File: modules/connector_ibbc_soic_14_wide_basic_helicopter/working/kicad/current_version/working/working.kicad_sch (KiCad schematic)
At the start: 1 part, among them U1 insoic14wi2cheli

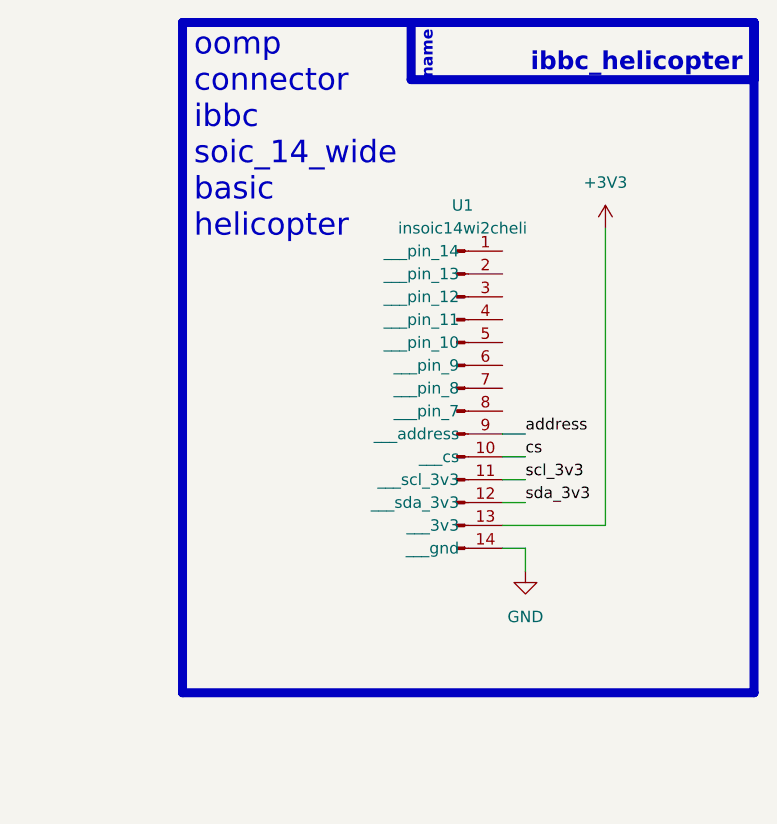
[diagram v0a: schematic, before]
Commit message: fixed formatting to be more consistent
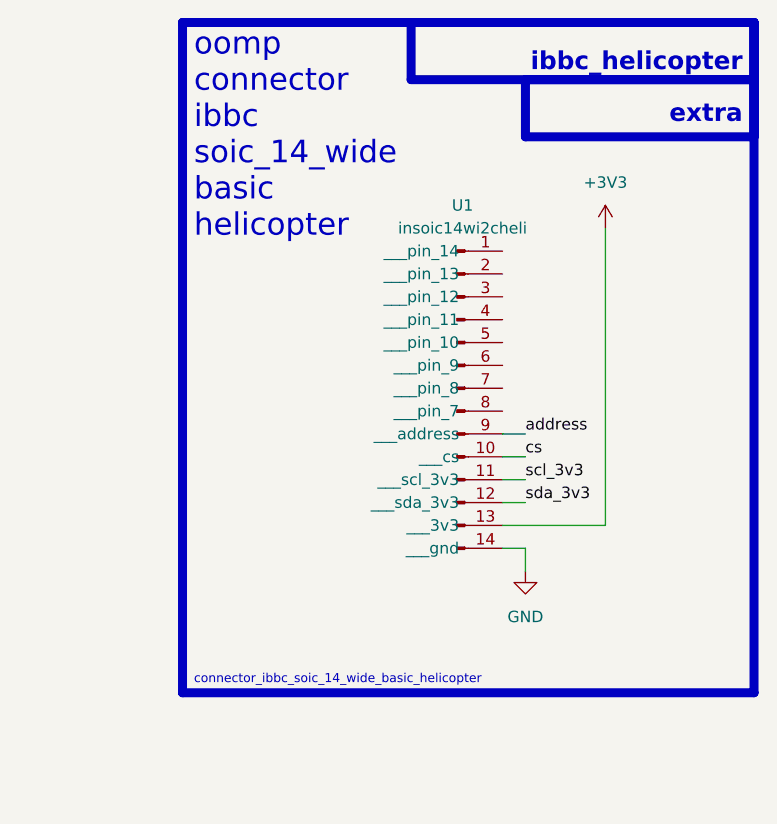
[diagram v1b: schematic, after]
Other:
- note added: "connector_ibbc_soic_14_wide_basic_helicopter"
- note added: "extra"
- note removed: "name"
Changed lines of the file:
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@@
     (stroke (width 0) (type default))
+  )
+  (rectangle (start 132.08 24.13) (end 157.48 30.48)
+    (stroke (width 1) (type default))
+    (fill (type none))
   )
   (rectangle (start 93.98 17.78) (end 157.48 92.2532)
@@
   (rectangle (start 119.38 17.78) (end 157.48 24.13)
     (stroke (width 1) (type default))
-    (fill (type color) (color 0 0 0 0))
+    (fill (type none))
   )
   (text "ibbc_helicopter\n\n" (at 156.21 26.67 0)
-    (effects (font (size 2 2) (thickness 0.8) bold (color 255 255 255 1)) (justify right bottom))
-  )
-  (text "name" (at 121.92 24.13 90)
-    (effects (font (size 1.27 1.27) (thickness 0.254) bold (color 255 255 255 1)) (justify left bottom))
+    (effects (font (size 2 2) (thickness 0.8) bold) (justify right bottom))
   )
   (text "oomp\nconnector\nibbc\nsoic_14_wide\nbasic\nhelicopter\n"
@@
     (effects (font (size 2.5 2.5)) (justify left bottom))
   )
+  (text "extra" (at 156.21 29.21 0)
+    (effects (font (size 2 2) (thickness 0.8) bold) (justify right bottom))
+  )
+  (text "connector_ibbc_soic_14_wide_basic_helicopter" (at 95.25 91.44 0)
+    (effects (font (size 1 1)) (justify left bottom))
+  )
   (label "cs" (at 132.08 66.04 0) (fields_autoplaced)

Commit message: schematic formatting
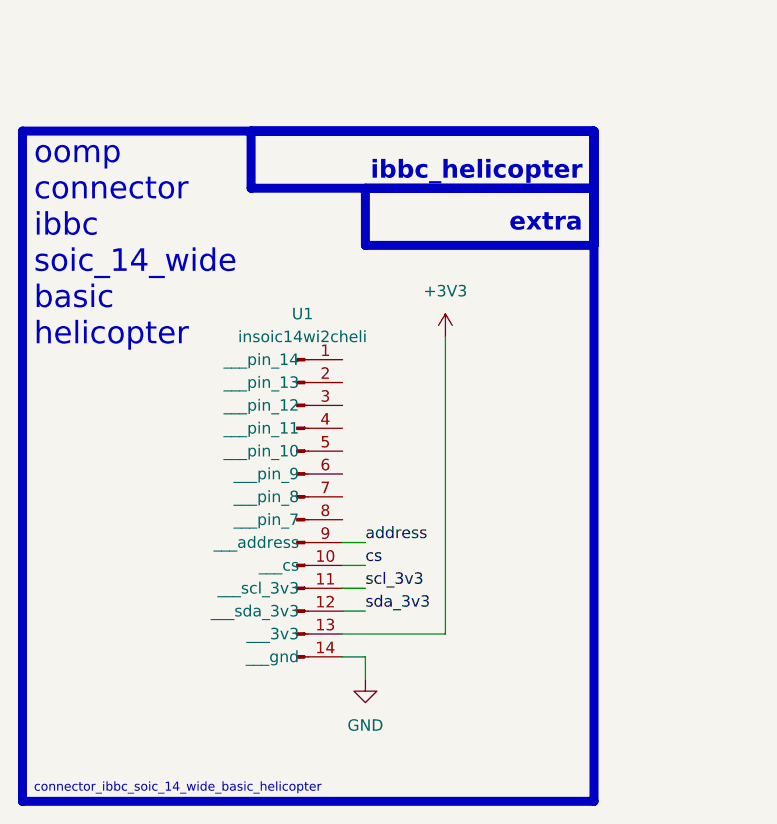
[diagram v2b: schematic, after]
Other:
- moved on the sheet: U1
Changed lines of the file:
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@@
 (kicad_sch (version 20230121) (generator eeschema)
-  (paper "A4")
-  (wire (pts (xy 140.97 73.66) (xy 129.54 73.66))
+  (paper "A5")
+  (wire (pts (xy 123.19 85.725) (xy 111.76 85.725))
     (stroke (width 0) (type default))
   )
-  (wire (pts (xy 129.54 66.04) (xy 132.08 66.04))
+  (wire (pts (xy 111.76 78.105) (xy 114.3 78.105))
     (stroke (width 0) (type default))
   )
-  (wire (pts (xy 129.54 63.5) (xy 132.08 63.5))
+  (wire (pts (xy 111.76 75.565) (xy 114.3 75.565))
     (stroke (width 0) (type default))
   )
-  (wire (pts (xy 140.97 40.64) (xy 140.97 73.66))
+  (wire (pts (xy 123.19 52.705) (xy 123.19 85.725))
     (stroke (width 0) (type default))
   )
-  (wire (pts (xy 129.54 71.12) (xy 132.08 71.12))
+  (wire (pts (xy 111.76 83.185) (xy 114.3 83.185))
     (stroke (width 0) (type default))
   )
-  (wire (pts (xy 132.08 76.2) (xy 129.54 76.2))
+  (wire (pts (xy 114.3 88.265) (xy 111.76 88.265))
     (stroke (width 0) (type default))
   )
-  (wire (pts (xy 132.08 78.74) (xy 132.08 76.2))
+  (wire (pts (xy 114.3 90.805) (xy 114.3 88.265))
     (stroke (width 0) (type default))
   )
-  (wire (pts (xy 129.54 68.58) (xy 132.08 68.58))
+  (wire (pts (xy 111.76 80.645) (xy 114.3 80.645))
     (stroke (width 0) (type default))
   )
-  (rectangle (start 132.08 24.13) (end 157.48 30.48)
+  (rectangle (start 114.3 36.195) (end 139.7 42.545)
     (stroke (width 1) (type default))
     (fill (type none))
   )
-  (rectangle (start 93.98 17.78) (end 157.48 92.2532)
+  (rectangle (start 76.2 29.845) (end 139.7 104.3182)
     (stroke (width 1) (type default))
     (fill (type none))
   )
-  (rectangle (start 119.38 17.78) (end 157.48 24.13)
+  (rectangle (start 101.6 29.845) (end 139.7 36.195)
     (stroke (width 1) (type default))
     (fill (type none))
   )
-  (text "ibbc_helicopter\n\n" (at 156.21 26.67 0)
+  (text "ibbc_helicopter\n\n" (at 138.43 38.735 0)
     (effects (font (size 2 2) (thickness 0.8) bold) (justify right bottom))
   )
   (text "oomp\nconnector\nibbc\nsoic_14_wide\nbasic\nhelicopter\n"
-    (at 95.25 41.91 0)
+    (at 77.47 53.975 0)
     (effects (font (size 2.5 2.5)) (justify left bottom))
   )
-  (text "extra" (at 156.21 29.21 0)
+  (text "extra" (at 138.43 41.275 0)
     (effects (font (size 2 2) (thickness 0.8) bold) (justify right bottom))
   )
-  (text "connector_ibbc_soic_14_wide_basic_helicopter" (at 95.25 91.44 0)
+  (text "connector_ibbc_soic_14_wide_basic_helicopter" (at 77.47 103.505 0)
     (effects (font (size 1 1)) (justify left bottom))
   )
-  (label "cs" (at 132.08 66.04 0) (fields_autoplaced)
+  (label "cs" (at 114.3 78.105 0) (fields_autoplaced)
     (effects (font (size 1.27 1.27)) (justify left bottom))
   )
-  (label "address" (at 132.08 63.5 0) (fields_autoplaced)
+  (label "address" (at 114.3 75.565 0) (fields_autoplaced)
     (effects (font (size 1.27 1.27)) (justify left bottom))
   )
-  (label "sda_3v3" (at 132.08 71.12 0) (fields_autoplaced)
+  (label "sda_3v3" (at 114.3 83.185 0) (fields_autoplaced)
     (effects (font (size 1.27 1.27)) (justify left bottom))
   )
-  (label "scl_3v3" (at 132.08 68.58 0) (fields_autoplaced)
+  (label "scl_3v3" (at 114.3 80.645 0) (fields_autoplaced)
     (effects (font (size 1.27 1.27)) (justify left bottom))
   )
-  (symbol (lib_id "oomlout_oomp_part_symbols:insoic14wi2cheli_electronic_interposer_soic_14_wide_i2c_helicopter") (at 124.46 58.42 0) (unit 1)
+  (symbol (lib_id "oomlout_oomp_part_symbols:insoic14wi2cheli_electronic_interposer_soic_14_wide_i2c_helicopter") (at 106.68 70.485 0) (unit 1)
     (in_bom yes) (on_board yes) (dnp no) (fields_autoplaced)
-    (property "Reference" "U1" (at 125.095 38.1 0)
+    (property "Reference" "U1" (at 107.315 50.165 0)
       (effects (font (size 1.27 1.27)))
     )
-    (property "Value" "insoic14wi2cheli" (at 125.095 40.64 0)
+    (property "Value" "insoic14wi2cheli" (at 107.315 52.705 0)
       (effects (font (size 1.27 1.27)))
     )
-    (property "Footprint" "oomlout_oomp_part_footprints:insoic14wi2cheli_electronic_interposer_soic_14_wide_i2c_helicopter" (at 124.46 58.42 0)
+    (property "Footprint" "oomlout_oomp_part_footprints:insoic14wi2cheli_electronic_interposer_soic_14_wide_i2c_helicopter" (at 106.68 70.485 0)
       (effects (font (size 1.27 1.27)) hide)
     )
-    (property "Datasheet" "https://github.com/oomlout/oomlout_oomp_v3/parts/electronic_interposer_soic_14_wide_i2c_helicopter/datasheet.pdf" (at 124.46 58.42 0)
+    (property "Datasheet" "https://github.com/oomlout/oomlout_oomp_v3/parts/electronic_interposer_soic_14_wide_i2c_helicopter/datasheet.pdf" (at 106.68 70.485 0)
       (effects (font (size 1.27 1.27)) hide)
     )
@@
     )
   )
-  (symbol (lib_id "power:GND") (at 132.08 78.74 0) (unit 1)
+  (symbol (lib_id "power:GND") (at 114.3 90.805 0) (unit 1)
     (in_bom yes) (on_board yes) (dnp no) (fields_autoplaced)
-    (property "Reference" "#PWR06" (at 132.08 85.09 0)
+    (property "Reference" "#PWR06" (at 114.3 97.155 0)
       (effects (font (size 1.27 1.27)) hide)
     )
-    (property "Value" "GND" (at 132.08 83.82 0)
+    (property "Value" "GND" (at 114.3 95.885 0)
       (effects (font (size 1.27 1.27)))
     )
-    (property "Footprint" "" (at 132.08 78.74 0)
+    (property "Footprint" "" (at 114.3 90.805 0)
       (effects (font (size 1.27 1.27)) hide)
     )
-    (property "Datasheet" "" (at 132.08 78.74 0)
+    (property "Datasheet" "" (at 114.3 90.805 0)
       (effects (font (size 1.27 1.27)) hide)
     )
@@
     )
   )
-  (symbol (lib_id "power:+3V3") (at 140.97 40.64 0) (unit 1)
+  (symbol (lib_id "power:+3V3") (at 123.19 52.705 0) (unit 1)
     (in_bom yes) (on_board yes) (dnp no) (fields_autoplaced)
-    (property "Reference" "#PWR05" (at 140.97 44.45 0)
+    (property "Reference" "#PWR05" (at 123.19 56.515 0)
       (effects (font (size 1.27 1.27)) hide)
     )
-    (property "Value" "+3V3" (at 140.97 35.56 0)
+    (property "Value" "+3V3" (at 123.19 47.625 0)
       (effects (font (size 1.27 1.27)))
     )
-    (property "Footprint" "" (at 140.97 40.64 0)
+    (property "Footprint" "" (at 123.19 52.705 0)
       (effects (font (size 1.27 1.27)) hide)
     )
-    (property "Datasheet" "" (at 140.97 40.64 0)
+    (property "Datasheet" "" (at 123.19 52.705 0)
       (effects (font (size 1.27 1.27)) hide)
     )
